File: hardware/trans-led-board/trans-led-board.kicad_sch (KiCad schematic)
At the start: 21 parts, among them J1 Conn_01x04, U1 MIC4812, U2 MIC4812

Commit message: Mounting holes shouldn't be in the BOM
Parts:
- FID1, FID2, FID3, H1, H2: now left out of the parts list
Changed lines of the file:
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@@
 		(unit 1)
 		(exclude_from_sim no)
-		(in_bom yes)
+		(in_bom no)
 		(on_board yes)
 		(dnp no)
@@
 		)
 		(property "Description" ""
+			(at 123.19 22.86 0)
+			(effects
+				(font
+					(size 1.27 1.27)
+				)
+				(hide yes)
+			)
+		)
+		(property "Manufacturer" ""
+			(at 123.19 22.86 0)
+			(effects
+				(font
+					(size 1.27 1.27)
+				)
+				(hide yes)
+			)
+		)
+		(property "Manufacturer PN" ""
+			(at 123.19 22.86 0)
+			(effects
+				(font
+					(size 1.27 1.27)
+				)
+				(hide yes)
+			)
+		)
+		(property "Supplier" ""
+			(at 123.19 22.86 0)
+			(effects
+				(font
+					(size 1.27 1.27)
+				)
+				(hide yes)
+			)
+		)
+		(property "Supplier PN" ""
 			(at 123.19 22.86 0)
 			(effects
@@
 		(unit 1)
 		(exclude_from_sim no)
-		(in_bom yes)
+		(in_bom no)
 		(on_board yes)
 		(dnp no)
@@
 		)
 		(property "Description" ""
+			(at 123.19 29.21 0)
+			(effects
+				(font
+					(size 1.27 1.27)
+				)
+				(hide yes)
+			)
+		)
+		(property "Manufacturer" ""
+			(at 123.19 29.21 0)
+			(effects
+				(font
+					(size 1.27 1.27)
+				)
+				(hide yes)
+			)
+		)
+		(property "Manufacturer PN" ""
+			(at 123.19 29.21 0)
+			(effects
+				(font
+					(size 1.27 1.27)
+				)
+				(hide yes)
+			)
+		)
+		(property "Supplier" ""
+			(at 123.19 29.21 0)
+			(effects
+				(font
+					(size 1.27 1.27)
+				)
+				(hide yes)
+			)
+		)
+		(property "Supplier PN" ""
 			(at 123.19 29.21 0)
 			(effects
@@
 		(unit 1)
 		(exclude_from_sim no)
-		(in_bom yes)
+		(in_bom no)
 		(on_board yes)
 		(dnp no)
@@
 		)
 		(property "Description" ""
+			(at 142.875 22.86 0)
+			(effects
+				(font
+					(size 1.27 1.27)
+				)
+				(hide yes)
+			)
+		)
+		(property "Manufacturer" ""
+			(at 142.875 22.86 0)
+			(effects
+				(font
+					(size 1.27 1.27)
+				)
+				(hide yes)
+			)
+		)
+		(property "Manufacturer PN" ""
+			(at 142.875 22.86 0)
+			(effects
+				(font
+					(size 1.27 1.27)
+				)
+				(hide yes)
+			)
+		)
+		(property "Supplier" ""
+			(at 142.875 22.86 0)
+			(effects
+				(font
+					(size 1.27 1.27)
+				)
+				(hide yes)
+			)
+		)
+		(property "Supplier PN" ""
 			(at 142.875 22.86 0)
 			(effects
@@
 		(unit 1)
 		(exclude_from_sim no)
-		(in_bom yes)
+		(in_bom no)
 		(on_board yes)
 		(dnp no)
@@
 		)
 		(property "Description" ""
+			(at 142.875 29.21 0)
+			(effects
+				(font
+					(size 1.27 1.27)
+				)
+				(hide yes)
+			)
+		)
+		(property "Manufacturer" ""
+			(at 142.875 29.21 0)
+			(effects
+				(font
+					(size 1.27 1.27)
+				)
+				(hide yes)
+			)
+		)
+		(property "Manufacturer PN" ""
+			(at 142.875 29.21 0)
+			(effects
+				(font
+					(size 1.27 1.27)
+				)
+				(hide yes)
+			)
+		)
+		(property "Supplier" ""
+			(at 142.875 29.21 0)
+			(effects
+				(font
+					(size 1.27 1.27)
+				)
+				(hide yes)
+			)
+		)
+		(property "Supplier PN" ""
 			(at 142.875 29.21 0)
 			(effects
@@
 		(unit 1)
 		(exclude_from_sim no)
-		(in_bom yes)
+		(in_bom no)
 		(on_board yes)
 		(dnp no)
@@
 			(at 142.875 35.56 0)
 			(effects
+				(font
+					(size 1.27 1.27)
+				)
+				(hide yes)
+			)
+		)
+		(property "Manufacturer" ""
+			(at 142.875 35.56 0)
+			(effects
+				(font
+					(size 1.27 1.27)
+				)
+				(hide yes)
+			)
+		)
+		(property "Manufacturer PN" ""
+			(at 142.875 35.56 0)
+			(effects
+				(font
+					(size 1.27 1.27)
+				)
+				(hide yes)
+			)
+		)
+		(property "Supplier" ""
+			(at 142.875 35.56 0)
+			(effects
+				(font
+					(size 1.27 1.27)
+				)
+				(hide yes)
+			)
+		)
+		(property "Supplier PN" ""
+			(at 142.875 35.56 0)
+			(effects

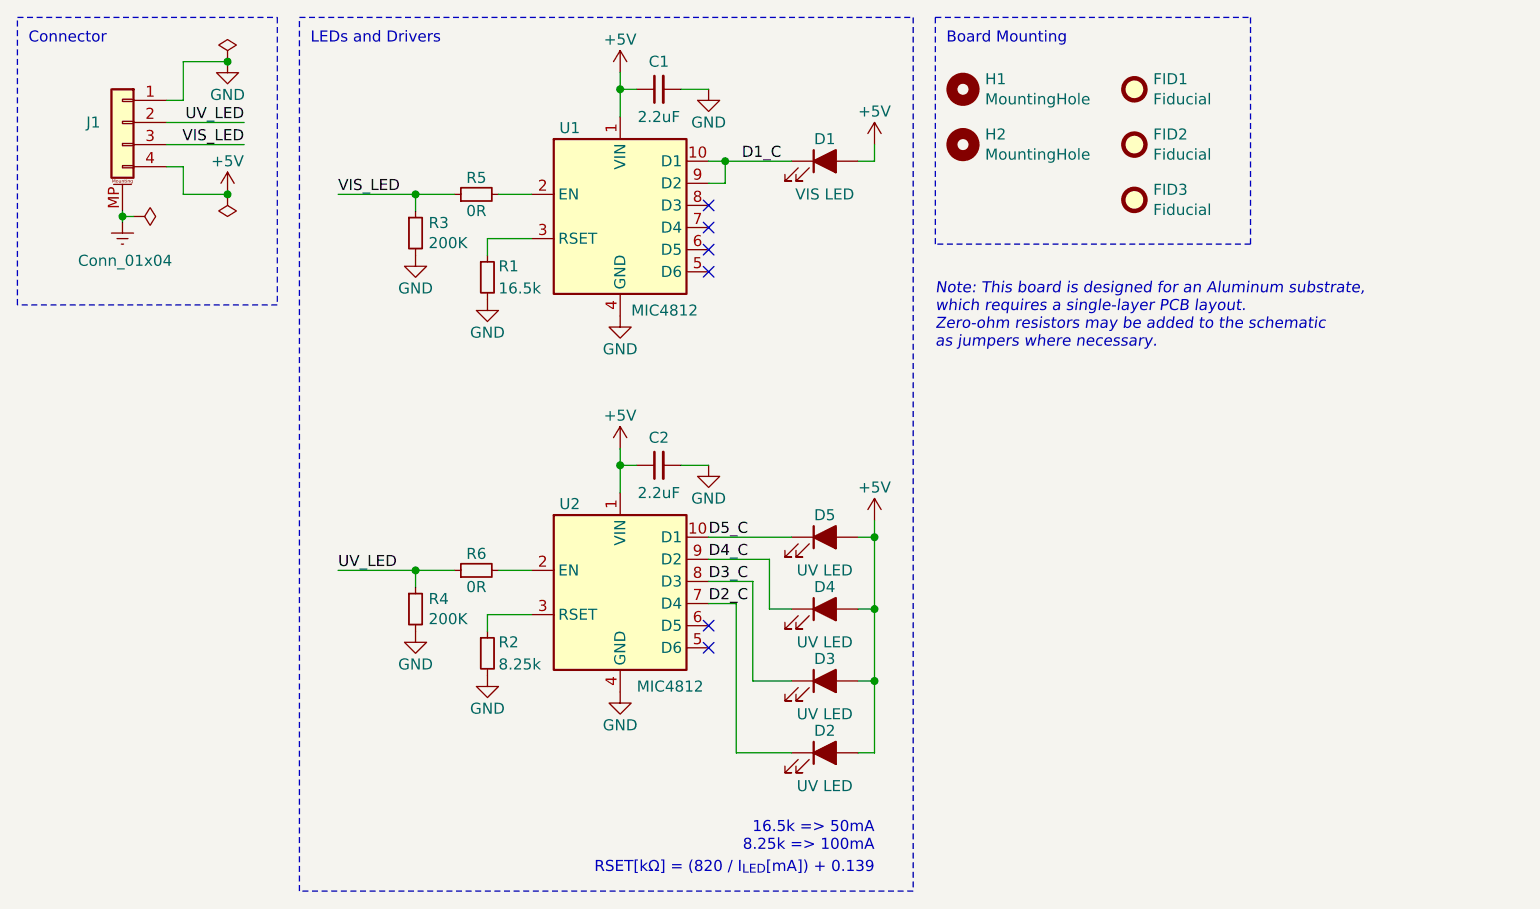
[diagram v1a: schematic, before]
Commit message: Change LED configuration on transmission board
Put four visible light LEDs on the outer ring, configured for 100mA each
Put a single higher-power UV LED in the center, configured for 400mA
Route things to maintain the same connector pin-out
Clean up board corners

Testing has shown that four corner LEDs only provide about 25% more
usable light than a single center LED, when all LEDs are run at the same
current level. (and this goes for both directions, and both visible and
UV)

Since we need as much UV light as possible, to overpower all of the
elements in the optical stack which attenuate UV light far more than
visible light, this configuration change allows us to dramatically
increase the amount of UV light for transmission measurements.

The main downside is that visible light measurements will now take 4x as
much current, while only getting 25% more light. However, this is still
within our current budget.

But in exchange, we can now use a significantly more powerful UV LED and
drive it with the maximum amount of current we have available, hopefully
improving measurement of high UV density materials.
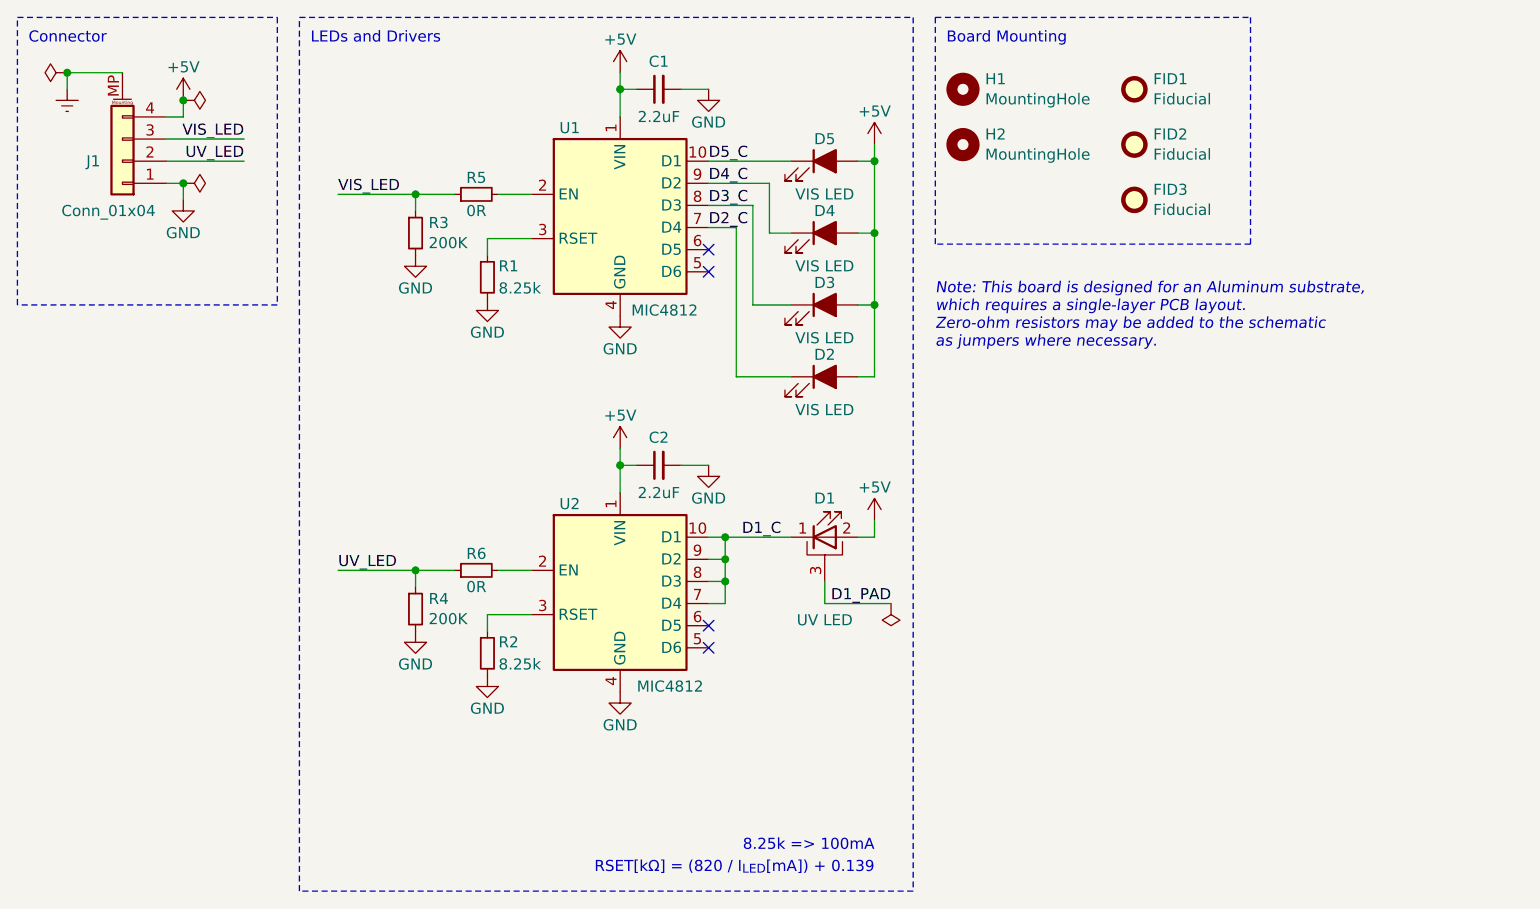
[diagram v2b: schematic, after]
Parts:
- D1: renamed from D2; footprint lib_fp:LED_WL-SUTW-2835_Narrow -> lib_fp:LED_Seoul_Z5; symbol Device:LED_Filled -> Device:LED_Pad; Manufacturer Würth Elektronik -> Seoul Viosys; Manufacturer PN 153283387A212 -> CUN86A1B; Supplier PN 732-153283387A212CT-ND -> 2112-CUN86A1BCT-ND
- D3, D4, D5: value UV LED -> VIS LED; footprint lib_fp:LED_WL-SUTW-2835_Narrow -> lib_fp:SunLike_LED_S1S0_Narrow; Manufacturer Würth Elektronik -> Seoul Semiconductor Inc.; Manufacturer PN 153283387A212 -> S1S0-3030309503-0000003S-0P001; Supplier PN 732-153283387A212CT-ND -> 897-S1S0-3030309503-0000003S-0P001CT-ND
- R1: value 16.5k -> 8.25k; Manufacturer TE Connectivity Passive Product -> Vishay Dale; Manufacturer PN CPF0603F16K5C1 -> CRCW06038K25FKEBC; Supplier Digi-Key -> Mouser; Supplier PN A102224CT-ND -> 71-CRCW06038K25FKEBC
- renumbered D1 to D2
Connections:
- net D1_C: now also D1.1 (K), U2.10 (D1), U2.7 (D4), U2.8 (D3), U2.9 (D2); no longer D2.1 (K), U1.10 (D1), U1.9 (D2)
- net D2_C: now also D2.1 (K), U1.7 (D4); no longer D1.1 (K), U2.7 (D4)
- net D3_C: now also U1.8 (D3); no longer U2.8 (D3)
- net D4_C: now also U1.9 (D2); no longer U2.9 (D2)
- net D5_C: now also U1.10 (D1); no longer U2.10 (D1)
- new net D1_PAD: D1.3 (PAD)
- no-connect marks 6 -> 4
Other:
- note added: "8.25k => 100mA"
- note removed: "16.5k => 50mA 8.25k => 100mA"
- moved on the sheet: D2, J1
